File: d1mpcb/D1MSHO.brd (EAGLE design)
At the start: 100 x 80 mm, 11 parts, among them T1 BD139

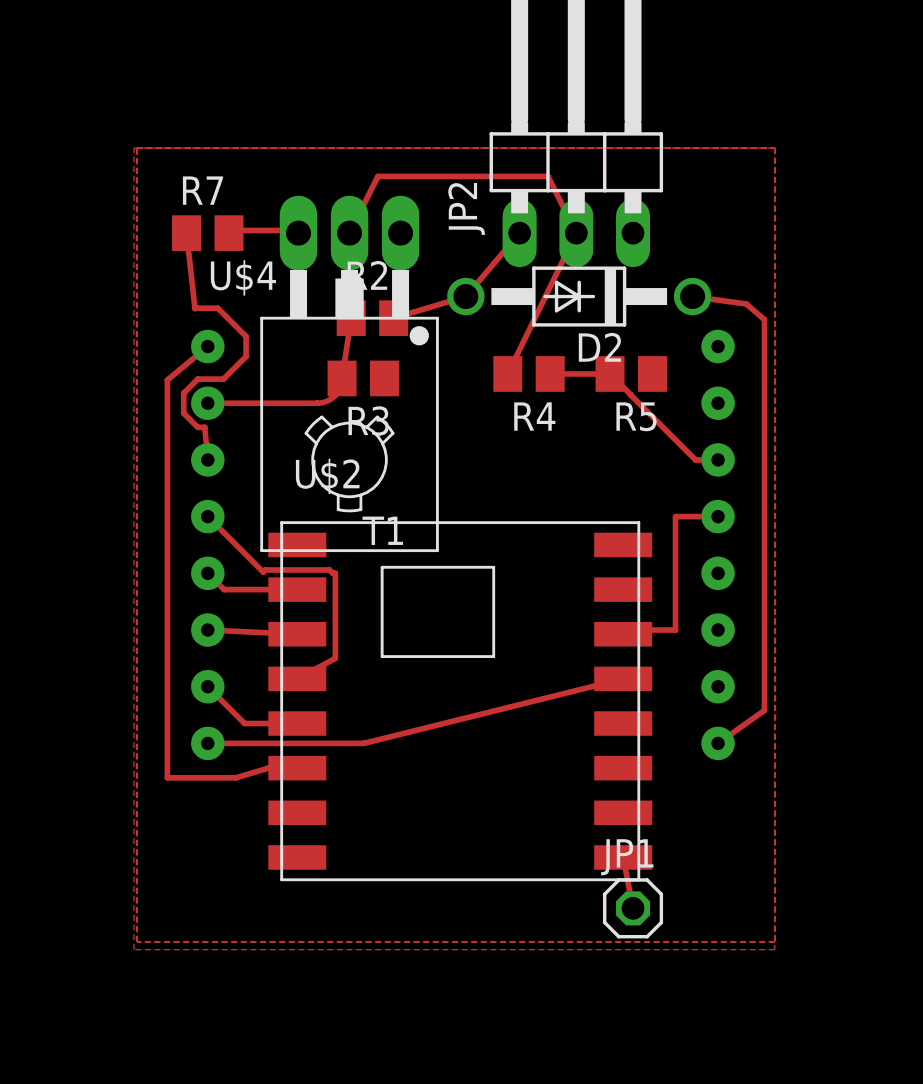
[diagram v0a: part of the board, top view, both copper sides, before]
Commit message: new schematic and rx driver
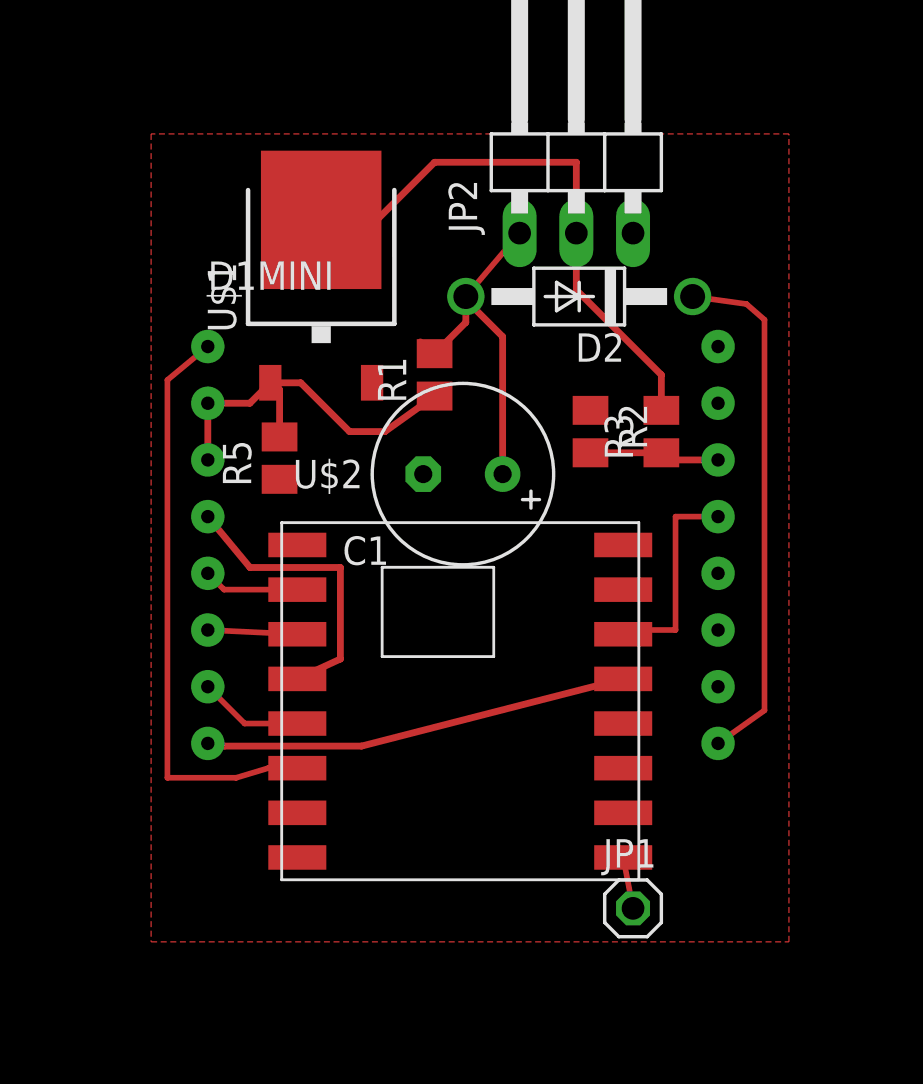
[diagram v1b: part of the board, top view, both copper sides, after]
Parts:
- removed R4: 39k, resistor:M0805
- removed R7: 12k, resistor:M0805
- removed T1: BD139, transistor:TO126
- added C1: (no value), resistor:E3,5-8
- added R1: 100k, resistor:M0805
- added U$1: FDD6635, fdd6635:TO252
- R3: value 33k -> 12k
- R5: value 12k -> 82k
- moved R5 16.2 mm to (38.8, 45.8), turned to 90 degrees
- moved R3 13.6 mm to (55.9, 47.0), turned to 90 degrees
- moved R2 11.0 mm to (52.7, 47.0), turned to 270 degrees
- renumbered U$4 to D1MINI
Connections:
- removed net D0: D1MINI.D0, R7.1
- removed net D1: D1MINI.D1, R4.1, R5.2
- net A0: now also D1MINI.D0, R1.1, R5.2, U$1.1; no longer R2.1, R3.2
- net GND: now also C1.-, R2.1, U$1.2; no longer R3.1, T1.1
- net N$1: now also R3.2, U$1.3; no longer R4.2, T1.2
- net N$2: now also D1MINI.D1, R2.2, R3.1; no longer R7.2, T1.3
- net N$3: now also C1.+, R1.2; no longer R2.2
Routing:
- net D0: track 14.2 -> 0.00 mm
- net N$3: track 7.10 -> 16.4 mm
- net D1: track 9.12 -> 0.00 mm
- net A0: track 9.21 -> 17.6 mm
- net N$1: track 20.4 -> 25.2 mm
- net N$2: track 3.18 -> 5.85 mm
- net D5: track 12.6 -> 13.2 mm
- removed copper zone on layer 1, net N$7
